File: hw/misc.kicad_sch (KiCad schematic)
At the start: 14 parts, among them Y1 Crystal_GND24

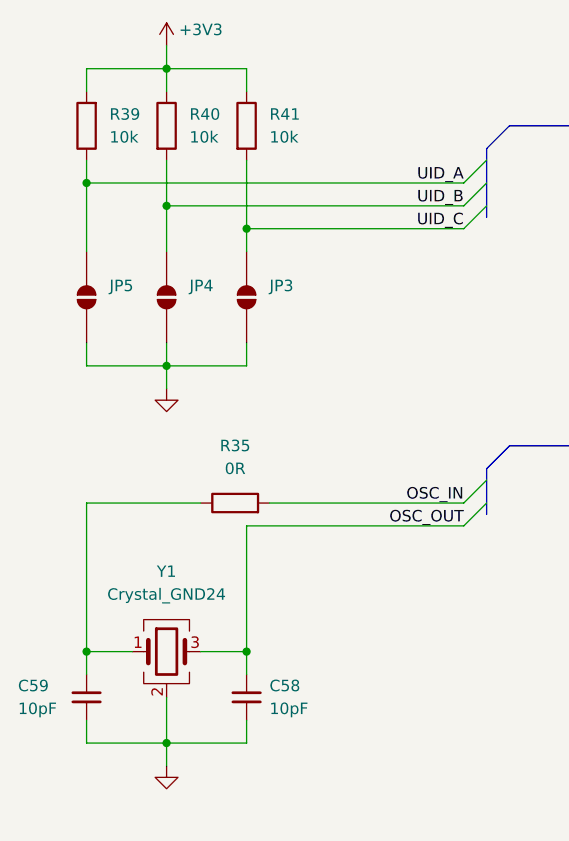
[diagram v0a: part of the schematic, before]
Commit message: began with lcsc and footprints
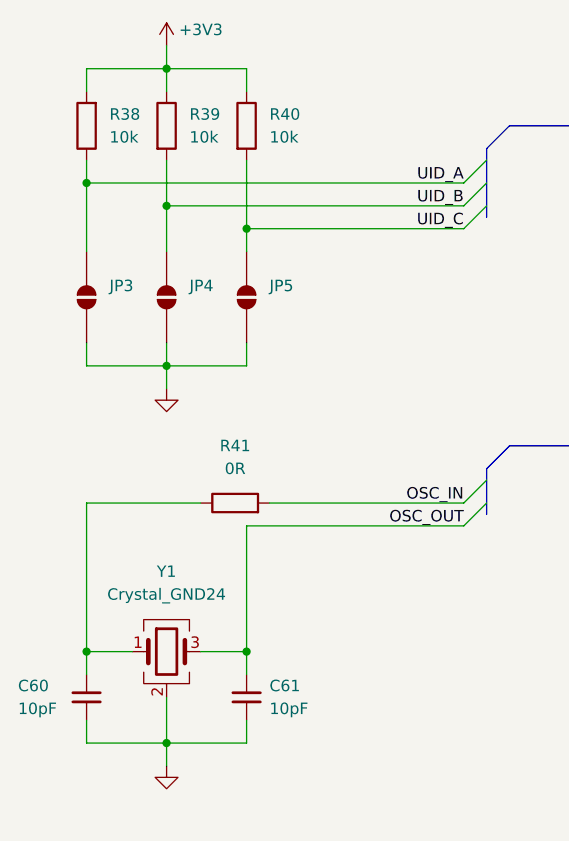
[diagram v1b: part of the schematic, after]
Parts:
- renumbered C59 to C60, C58 to C61, JP5 to JP3, JP3 to JP5, R39 to R38, R40 to R39, R41 to R40, R35 to R41
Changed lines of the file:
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@@
 		(dnp no)
 		(fields_autoplaced yes)
-		(property "Reference" "R41"
+		(property "Reference" "R40"
 			(at 147.32 59.6899 0)
 			(show_name no)
@@
 			(project "atlas-electronics"
 				(path "/915bc1ff-7be5-4368-a2db-c4889af73afd/d98e9200-e700-4901-ae61-391ae6250990"
-					(reference "R41")
+					(reference "R40")
 					(unit 1)
 				)
@@
 		(dnp no)
 		(fields_autoplaced yes)
-		(property "Reference" "#PWR072"
+		(property "Reference" "#PWR078"
 			(at 135.89 138.43 0)
 			(hide yes)
@@
 			(project "atlas-electronics"
 				(path "/915bc1ff-7be5-4368-a2db-c4889af73afd/d98e9200-e700-4901-ae61-391ae6250990"
-					(reference "#PWR072")
+					(reference "#PWR078")
 					(unit 1)
 				)
@@
 		(dnp no)
 		(fields_autoplaced yes)
-		(property "Reference" "#PWR068"
+		(property "Reference" "#PWR075"
 			(at 205.74 127 0)
 			(hide yes)
@@
 			(project "atlas-electronics"
 				(path "/915bc1ff-7be5-4368-a2db-c4889af73afd/d98e9200-e700-4901-ae61-391ae6250990"
-					(reference "#PWR068")
+					(reference "#PWR075")
 					(unit 1)
 				)
@@
 		(dnp no)
 		(fields_autoplaced yes)
-		(property "Reference" "#PWR073"
+		(property "Reference" "#PWR074"
 			(at 135.89 96.52 0)
 			(hide yes)
@@
 			(project "atlas-electronics"
 				(path "/915bc1ff-7be5-4368-a2db-c4889af73afd/d98e9200-e700-4901-ae61-391ae6250990"
-					(reference "#PWR073")
+					(reference "#PWR074")
 					(unit 1)
 				)
@@
 		(dnp no)
 		(fields_autoplaced yes)
-		(property "Reference" "JP3"
+		(property "Reference" "JP5"
 			(at 147.32 78.7399 90)
 			(show_name no)
@@
 			(project "atlas-electronics"
 				(path "/915bc1ff-7be5-4368-a2db-c4889af73afd/d98e9200-e700-4901-ae61-391ae6250990"
-					(reference "JP3")
+					(reference "JP5")
 					(unit 1)
 				)
@@
 		(dnp no)
 		(fields_autoplaced yes)
-		(property "Reference" "R35"
+		(property "Reference" "R41"
 			(at 143.51 96.52 90)
 			(show_name no)
@@
 			(project "atlas-electronics"
 				(path "/915bc1ff-7be5-4368-a2db-c4889af73afd/d98e9200-e700-4901-ae61-391ae6250990"
-					(reference "R35")
+					(reference "R41")
 					(unit 1)
 				)
@@
 		(dnp no)
 		(fields_autoplaced yes)
-		(property "Reference" "JP5"
+		(property "Reference" "JP3"
 			(at 129.54 78.7399 90)
 			(show_name no)
@@
 			(project "atlas-electronics"
 				(path "/915bc1ff-7be5-4368-a2db-c4889af73afd/d98e9200-e700-4901-ae61-391ae6250990"
-					(reference "JP5")
+					(reference "JP3")
 					(unit 1)
 				)
@@
 		(dnp no)
 		(fields_autoplaced yes)
-		(property "Reference" "#PWR070"
+		(property "Reference" "#PWR077"
 			(at 215.9 137.16 0)
 			(hide yes)
@@
 			(project "atlas-electronics"
 				(path "/915bc1ff-7be5-4368-a2db-c4889af73afd/d98e9200-e700-4901-ae61-391ae6250990"
-					(reference "#PWR070")
+					(reference "#PWR077")
 					(unit 1)
 				)
@@
 		(dnp no)
 		(fields_autoplaced yes)
-		(property "Reference" "R40"
+		(property "Reference" "R39"
 			(at 138.43 59.6899 0)
 			(show_name no)
@@
 			(project "atlas-electronics"
 				(path "/915bc1ff-7be5-4368-a2db-c4889af73afd/d98e9200-e700-4901-ae61-391ae6250990"
-					(reference "R40")
+					(reference "R39")
 					(unit 1)
 				)
@@
 		(dnp no)
 		(fields_autoplaced yes)
-		(property "Reference" "#PWR069"
+		(property "Reference" "#PWR076"
 			(at 210.82 132.08 0)
 			(hide yes)
@@
 			(project "atlas-electronics"
 				(path "/915bc1ff-7be5-4368-a2db-c4889af73afd/d98e9200-e700-4901-ae61-391ae6250990"
-					(reference "#PWR069")
+					(reference "#PWR076")
 					(unit 1)
 				)
@@
 		(dnp no)
 		(fields_autoplaced yes)
-		(property "Reference" "#PWR071"
+		(property "Reference" "#PWR079"
 			(at 220.98 142.24 0)
 			(hide yes)
@@
 			(project "atlas-electronics"
 				(path "/915bc1ff-7be5-4368-a2db-c4889af73afd/d98e9200-e700-4901-ae61-391ae6250990"
-					(reference "#PWR071")
+					(reference "#PWR079")
 					(unit 1)
 				)
@@
 		(dnp no)
 		(fields_autoplaced yes)
-		(property "Reference" "R39"
+		(property "Reference" "R38"
 			(at 129.54 59.6899 0)
 			(show_name no)
@@
 			(project "atlas-electronics"
 				(path "/915bc1ff-7be5-4368-a2db-c4889af73afd/d98e9200-e700-4901-ae61-391ae6250990"
-					(reference "R39")
+					(reference "R38")
 					(unit 1)
 				)
@@
 		(in_pos_files yes)
 		(dnp no)
-		(property "Reference" "C59"
+		(property "Reference" "C60"
 			(at 119.38 123.19 0)
 			(show_name no)
@@
 			(project "atlas-electronics"
 				(path "/915bc1ff-7be5-4368-a2db-c4889af73afd/d98e9200-e700-4901-ae61-391ae6250990"
-					(reference "C59")
+					(reference "C60")
 					(unit 1)
 				)
@@
 		(in_pos_files yes)
 		(dnp no)
-		(property "Reference" "#PWR074"
+		(property "Reference" "#PWR073"
 			(at 135.89 55.88 0)
 			(hide yes)
@@
 			(project "atlas-electronics"
 				(path "/915bc1ff-7be5-4368-a2db-c4889af73afd/d98e9200-e700-4901-ae61-391ae6250990"
-					(reference "#PWR074")
+					(reference "#PWR073")
 					(unit 1)
 				)
@@
 		(dnp no)
 		(fields_autoplaced yes)
-		(property "Reference" "C58"
+		(property "Reference" "C61"
 			(at 147.32 123.1899 0)
 			(show_name no)
@@
 			(project "atlas-electronics"
 				(path "/915bc1ff-7be5-4368-a2db-c4889af73afd/d98e9200-e700-4901-ae61-391ae6250990"
-					(reference "C58")
-					(unit 1)
-				)
+					(reference "C61")
+					(unit 1)
+				)

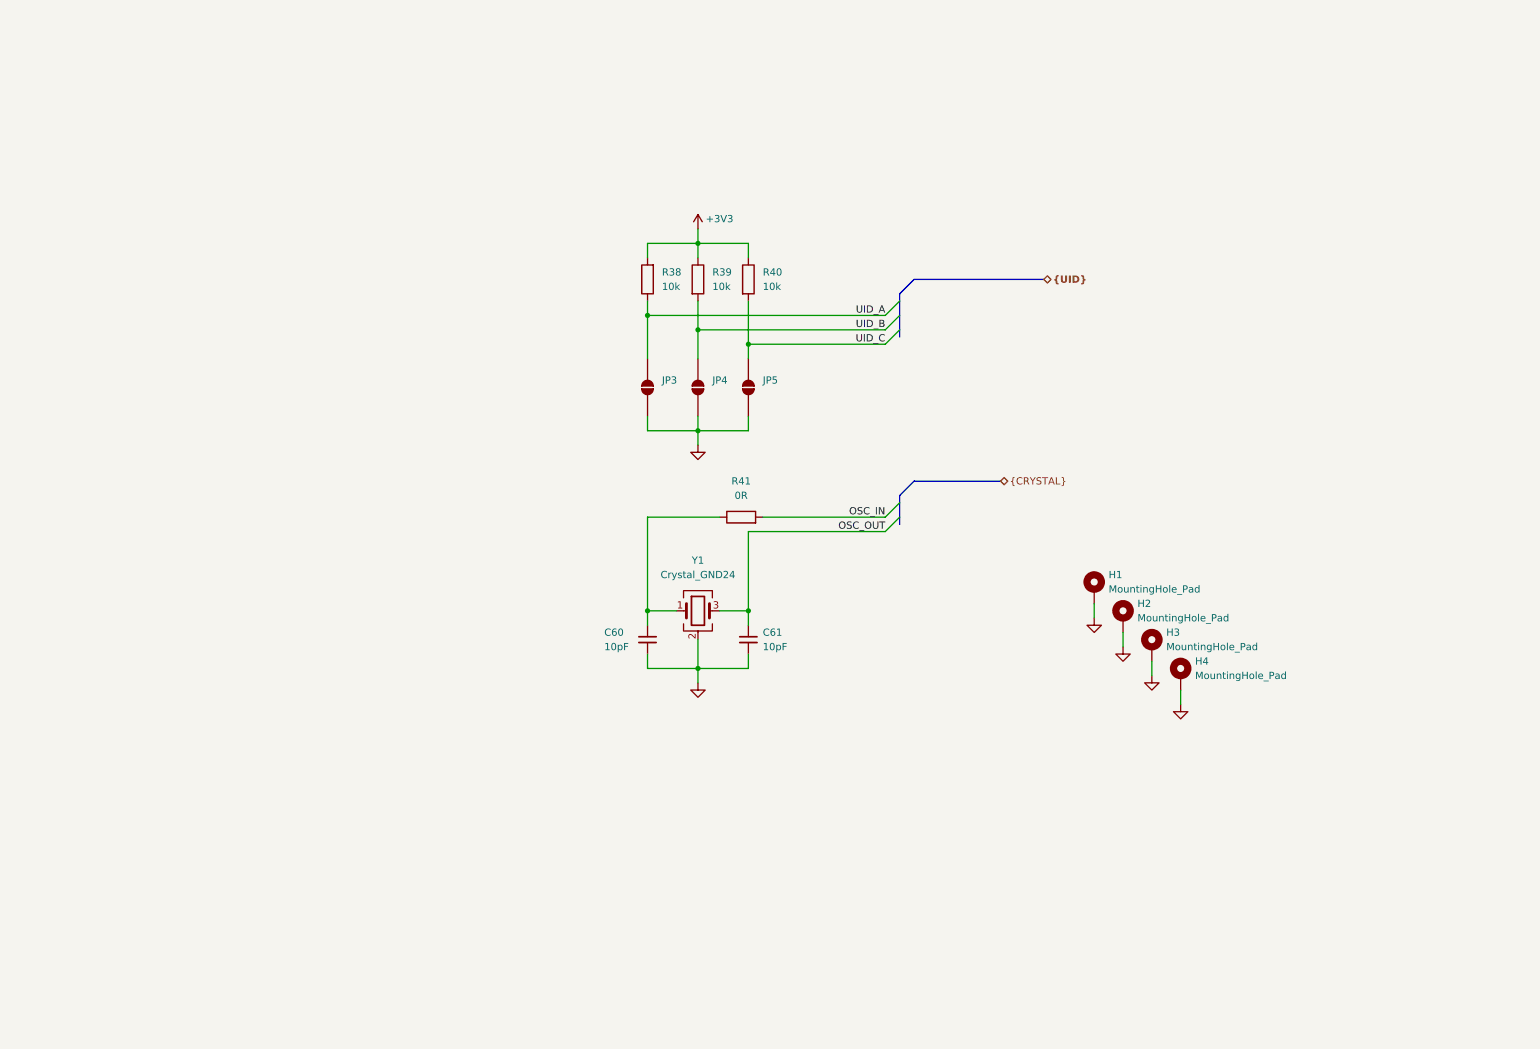
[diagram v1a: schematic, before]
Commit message: cleaned up *.kicad_sch
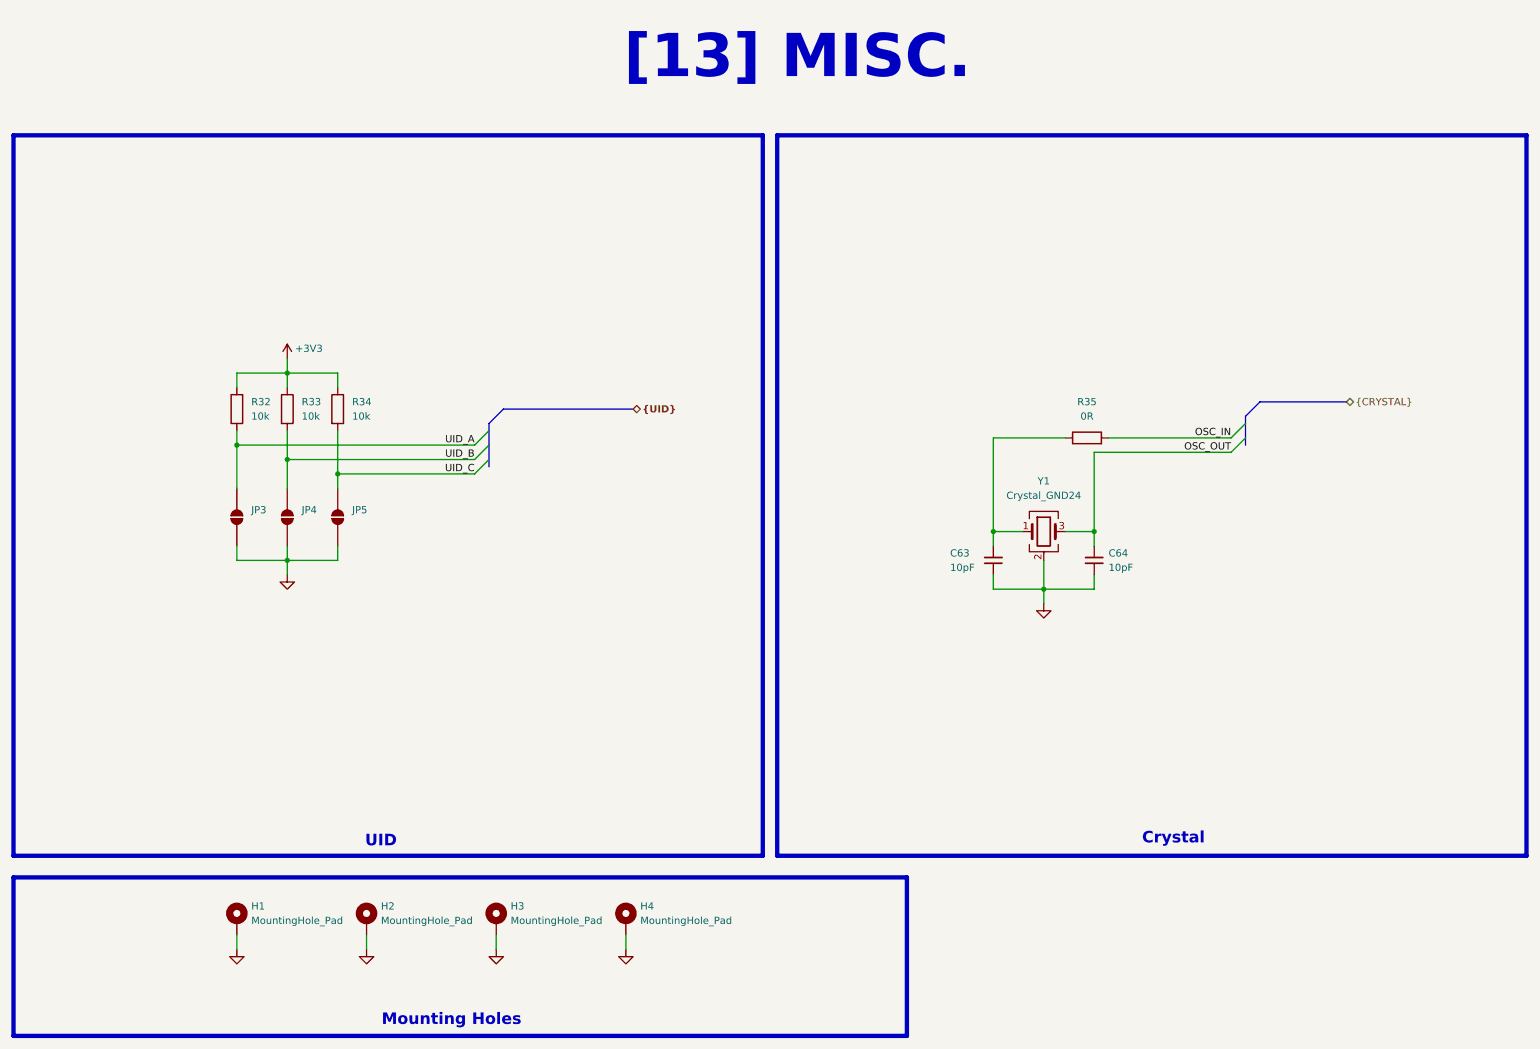
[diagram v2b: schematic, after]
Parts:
- renumbered C60 to C63, C61 to C64, R38 to R32, R39 to R33, R40 to R34, R41 to R35
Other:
- note added: "Crystal"
- note added: "Mounting Holes"
- note added: "UID"
- note added: "[13] MISC."
- moved on the sheet: C63, C64, JP3, JP4, JP5, R32, R33, R34, R35, Y1
